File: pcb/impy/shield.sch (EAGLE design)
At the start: 117 parts, among them J1 USB-2410-06, J2 SI-60062-F, J3 5V, U1 AD5933YRS, U10 LTC3406AB, U11 23LCV1024-I/SN, U12 MIC2009A-1YM6, U13 ADG725BSU, U14 ADG725BSU, U2 ADG704BRM, U3 AD8656ARZ, U4 M24C08WMN, U5 ADG706BRU, U6 DP83848I, U7 MIC2009A-1YM6, U8 AT25DF081A-SS, U9 SST25VF080B-80-4I-S2

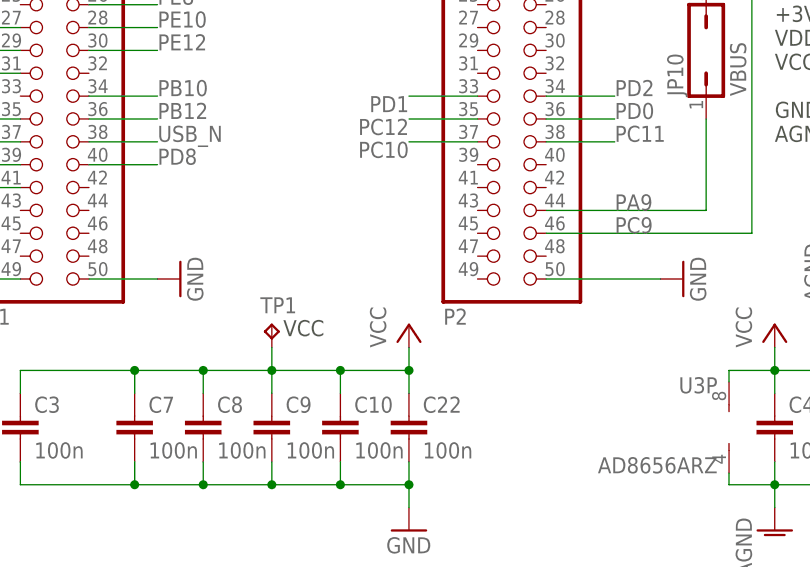
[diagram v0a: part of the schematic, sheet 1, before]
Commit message: * pcb/impy: (shield.sch) Fix missing ground connection on discovery connector.
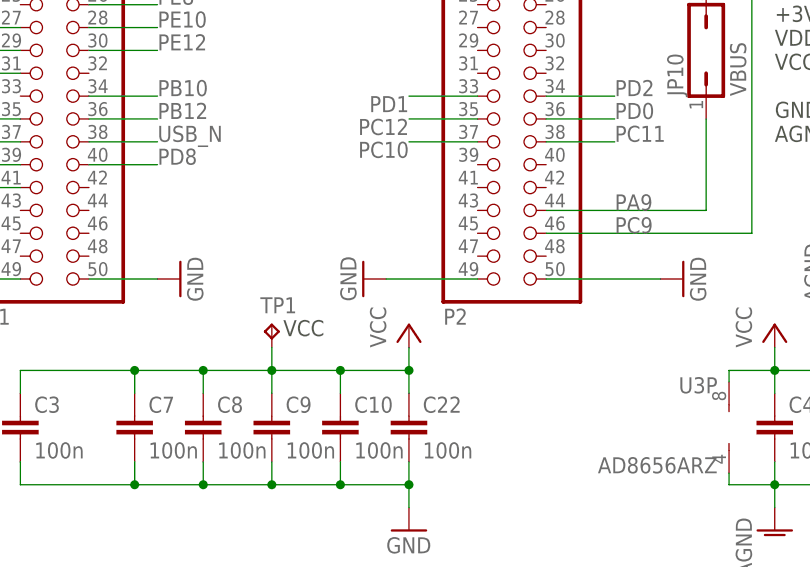
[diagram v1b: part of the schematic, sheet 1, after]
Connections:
- net GND: now also JP2.49
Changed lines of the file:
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@@
 <part name="P+36" library="supply1" deviceset="+5V" device=""/>
 <part name="VDD7" library="supply1" deviceset="VDD" device=""/>
+<part name="GND45" library="supply1" deviceset="GND" device=""/>
 </parts>
 <sheets>
@@
 <attribute name="VALUE" x="-2.54" y="17.78" size="1.778" layer="96" rot="MR180"/>
 </instance>
+<instance part="GND45" gate="1" x="58.42" y="20.32" rot="R270"/>
 </instances>
 <busses>
@@
 <wire x1="200.66" y1="-5.08" x2="200.66" y2="0" width="0.1524" layer="91"/>
 </segment>
+<segment>
+<pinref part="GND45" gate="1" pin="GND"/>
+<pinref part="JP2" gate="A" pin="49"/>
+<wire x1="60.96" y1="20.32" x2="71.12" y2="20.32" width="0.1524" layer="91"/>
+</segment>
 </net>

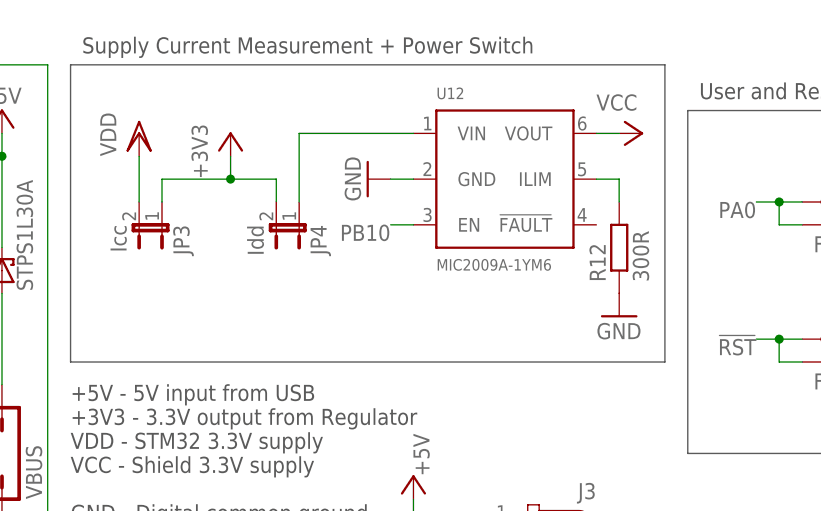
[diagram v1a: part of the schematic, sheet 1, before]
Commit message: * pcb/impy: (shield.sch) Move Icc measurement jumper after switch for easier layout.
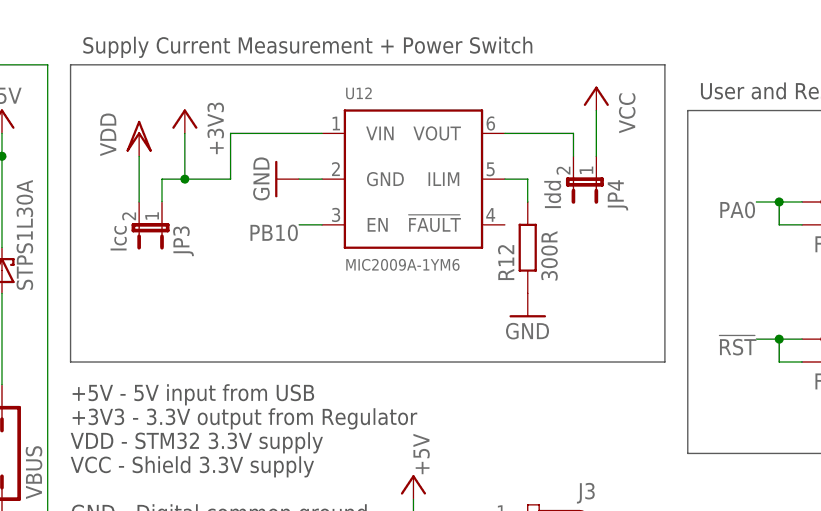
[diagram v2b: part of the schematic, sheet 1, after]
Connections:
- net +3V3: now also U12.VIN; no longer JP4.2
- net N$36: now also JP4.2, U12.VOUT; no longer JP4.1, U12.VIN
- net VCC: now also JP4.1; no longer U12.VOUT
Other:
- moved on the sheet: JP4, R12, U12
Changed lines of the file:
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@@
 <instance part="GND9" gate="1" x="60.96" y="81.28" rot="R270"/>
 <instance part="JP3" gate="A" x="114.3" y="71.12" rot="R180"/>
-<instance part="JP4" gate="A" x="129.54" y="71.12" rot="R180"/>
-<instance part="P+5" gate="VCC" x="167.64" y="81.28" smashed="yes" rot="R270">
-<attribute name="VALUE" x="162.56" y="83.82" size="1.778" layer="96"/>
+<instance part="JP4" gate="A" x="162.56" y="76.2" rot="R180"/>
+<instance part="P+5" gate="VCC" x="162.56" y="86.36" smashed="yes" rot="MR0">
+<attribute name="VALUE" x="165.1" y="81.28" size="1.778" layer="96" rot="MR90"/>
 </instance>
-<instance part="+3V3" gate="G$1" x="121.92" y="81.28"/>
+<instance part="+3V3" gate="G$1" x="116.84" y="83.82" rot="MR0"/>
 <instance part="VDD4" gate="G$1" x="111.76" y="81.28"/>
 <instance part="SJ1" gate="1" x="119.38" y="27.94"/>
@@
 <instance part="J3" gate="G$1" x="154.94" y="35.56" rot="MR0"/>
 <instance part="GND39" gate="1" x="147.32" y="27.94"/>
-<instance part="U12" gate="G$1" x="152.4" y="76.2"/>
-<instance part="GND35" gate="1" x="137.16" y="76.2" rot="R270"/>
+<instance part="U12" gate="G$1" x="142.24" y="76.2"/>
+<instance part="GND35" gate="1" x="127" y="76.2" rot="R270"/>
 <instance part="D1" gate="G$1" x="96.52" y="66.04" rot="R90"/>
-<instance part="R12" gate="G$1" x="165.1" y="68.58" smashed="yes" rot="R90">
-<attribute name="NAME" x="163.6014" y="64.77" size="1.778" layer="95" rot="R90"/>
-<attribute name="VALUE" x="168.402" y="64.77" size="1.778" layer="96" rot="R90"/>
+<instance part="R12" gate="G$1" x="154.94" y="68.58" smashed="yes" rot="R90">
+<attribute name="NAME" x="153.4414" y="64.77" size="1.778" layer="95" rot="R90"/>
+<attribute name="VALUE" x="158.242" y="64.77" size="1.778" layer="96" rot="R90"/>
 </instance>
-<instance part="GND40" gate="1" x="165.1" y="60.96"/>
+<instance part="GND40" gate="1" x="154.94" y="60.96"/>
 <instance part="U10" gate="G$1" x="167.64" y="15.24"/>
 <instance part="R14" gate="G$1" x="187.96" y="15.24" smashed="yes">
@@
 <pinref part="U12" gate="G$1" pin="GND"/>
 <pinref part="GND35" gate="1" pin="GND"/>
-<wire x1="142.24" y1="76.2" x2="139.7" y2="76.2" width="0.1524" layer="91"/>
+<wire x1="132.08" y1="76.2" x2="129.54" y2="76.2" width="0.1524" layer="91"/>
 </segment>
 <segment>
@@
 <wire x1="114.3" y1="73.66" x2="114.3" y2="76.2" width="0.1524" layer="91"/>
 <pinref part="+3V3" gate="G$1" pin="+3V3"/>
-<wire x1="114.3" y1="76.2" x2="121.92" y2="76.2" width="0.1524" layer="91"/>
-<wire x1="121.92" y1="76.2" x2="121.92" y2="78.74" width="0.1524" layer="91"/>
-<pinref part="JP4" gate="A" pin="2"/>
-<wire x1="121.92" y1="76.2" x2="127" y2="76.2" width="0.1524" layer="91"/>
-<wire x1="127" y1="76.2" x2="127" y2="73.66" width="0.1524" layer="91"/>
-<junction x="121.92" y="76.2"/>
+<wire x1="114.3" y1="76.2" x2="116.84" y2="76.2" width="0.1524" layer="91"/>
+<wire x1="116.84" y1="76.2" x2="116.84" y2="81.28" width="0.1524" layer="91"/>
+<wire x1="116.84" y1="76.2" x2="121.92" y2="76.2" width="0.1524" layer="91"/>
+<junction x="116.84" y="76.2"/>
+<pinref part="U12" gate="G$1" pin="VIN"/>
+<wire x1="132.08" y1="81.28" x2="121.92" y2="81.28" width="0.1524" layer="91"/>
+<wire x1="121.92" y1="81.28" x2="121.92" y2="76.2" width="0.1524" layer="91"/>
 </segment>
 <segment>
@@
 <segment>
 <pinref part="P+5" gate="VCC" pin="VCC"/>
-<pinref part="U12" gate="G$1" pin="VOUT"/>
-<wire x1="165.1" y1="81.28" x2="162.56" y2="81.28" width="0.1524" layer="91"/>
+<pinref part="JP4" gate="A" pin="1"/>
+<wire x1="162.56" y1="83.82" x2="162.56" y2="78.74" width="0.1524" layer="91"/>
 </segment>
 </net>
@@
 </segment>
 </net>
-<net name="N$36" class="1">
-<segment>
-<pinref part="U12" gate="G$1" pin="VIN"/>
-<pinref part="JP4" gate="A" pin="1"/>
-<wire x1="142.24" y1="81.28" x2="129.54" y2="81.28" width="0.1524" layer="91"/>
-<wire x1="129.54" y1="81.28" x2="129.54" y2="73.66" width="0.1524" layer="91"/>
-</segment>
-</net>
 <net name="PB10" class="0">
 <segment>
@@
 <segment>
 <pinref part="U12" gate="G$1" pin="EN"/>
-<wire x1="142.24" y1="71.12" x2="139.7" y2="71.12" width="0.1524" layer="91"/>
-<label x="139.7" y="71.12" size="1.778" layer="95" rot="R180"/>
+<wire x1="132.08" y1="71.12" x2="129.54" y2="71.12" width="0.1524" layer="91"/>
+<label x="129.54" y="71.12" size="1.778" layer="95" rot="R180"/>
 </segment>
 </net>
@@
 <pinref part="U12" gate="G$1" pin="ILIM"/>
 <pinref part="R12" gate="G$1" pin="2"/>
-<wire x1="162.56" y1="76.2" x2="165.1" y2="76.2" width="0.1524" layer="91"/>
-<wire x1="165.1" y1="76.2" x2="165.1" y2="73.66" width="0.1524" layer="91"/>
+<wire x1="152.4" y1="76.2" x2="154.94" y2="76.2" width="0.1524" layer="91"/>
+<wire x1="154.94" y1="76.2" x2="154.94" y2="73.66" width="0.1524" layer="91"/>
 </segment>
 </net>
@@
 </segment>
 </net>
+<net name="N$36" class="0">
+<segment>
+<pinref part="U12" gate="G$1" pin="VOUT"/>
+<pinref part="JP4" gate="A" pin="2"/>
+<wire x1="152.4" y1="81.28" x2="160.02" y2="81.28" width="0.1524" layer="91"/>
+<wire x1="160.02" y1="81.28" x2="160.02" y2="78.74" width="0.1524" layer="91"/>
+</segment>
+</net>

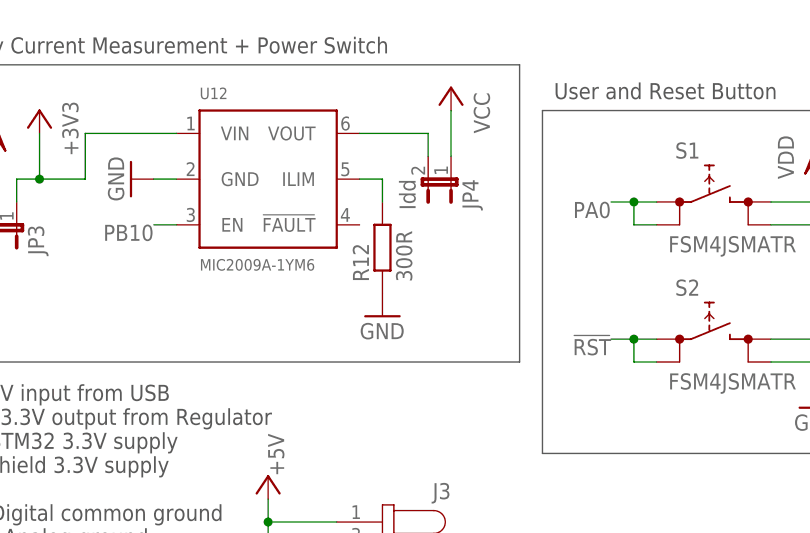
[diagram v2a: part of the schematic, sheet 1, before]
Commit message: * pcb/impy: (shield.sch) Change value of main power switch current limit resistor (to 510R which sets a 400mA limit). This switch does not carry the USB power, so the limit need not be that high.
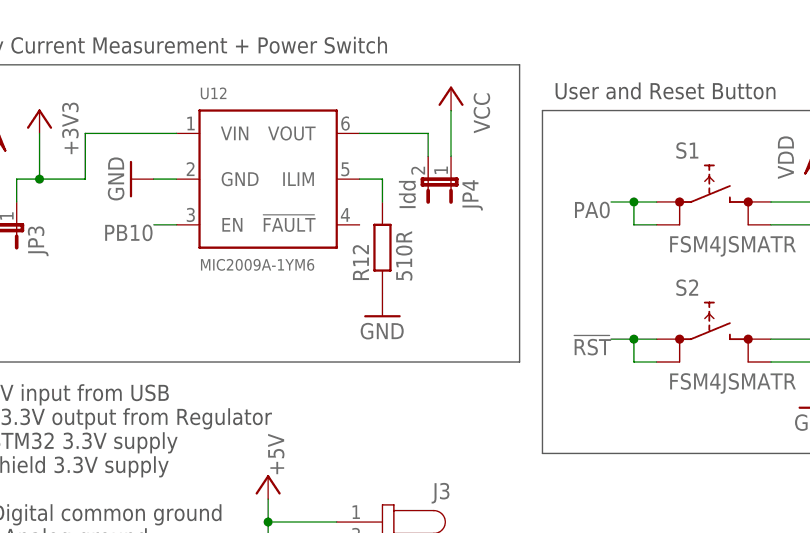
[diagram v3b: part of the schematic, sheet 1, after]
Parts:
- R12: value 300R -> 510R
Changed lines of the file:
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@@
 <part name="GND35" library="supply1" deviceset="GND" device=""/>
 <part name="D1" library="parts" deviceset="STPS1L30" device="A"/>
-<part name="R12" library="rcl" deviceset="R-EU_" device="R0603" value="300R"/>
+<part name="R12" library="rcl" deviceset="R-EU_" device="R0603" value="510R"/>
 <part name="GND40" library="supply1" deviceset="GND" device=""/>
 <part name="GND41" library="supply1" deviceset="GND" device=""/>

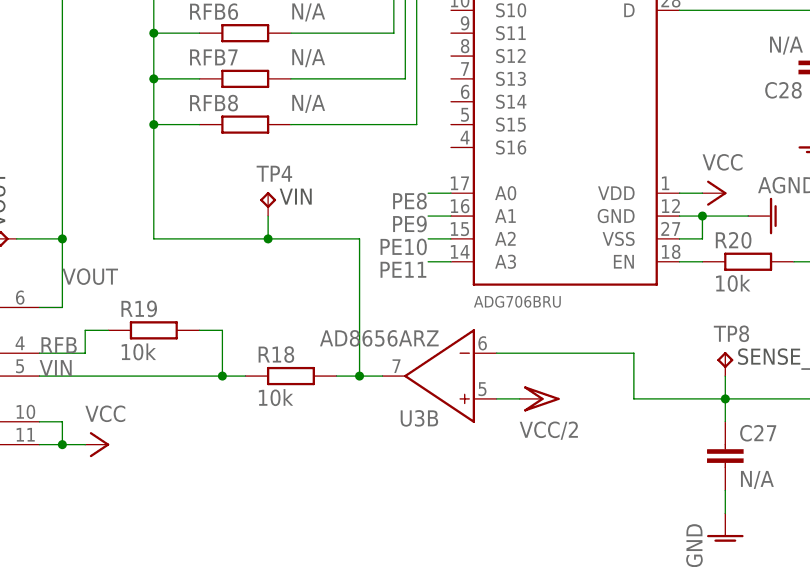
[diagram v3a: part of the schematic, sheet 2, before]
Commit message: * pcb/impy: (shield.sch) Remove unnecessary feedback resistor selection signal (PE11).   (shield.brd) Remove PE11 trace and straighten some other ones.
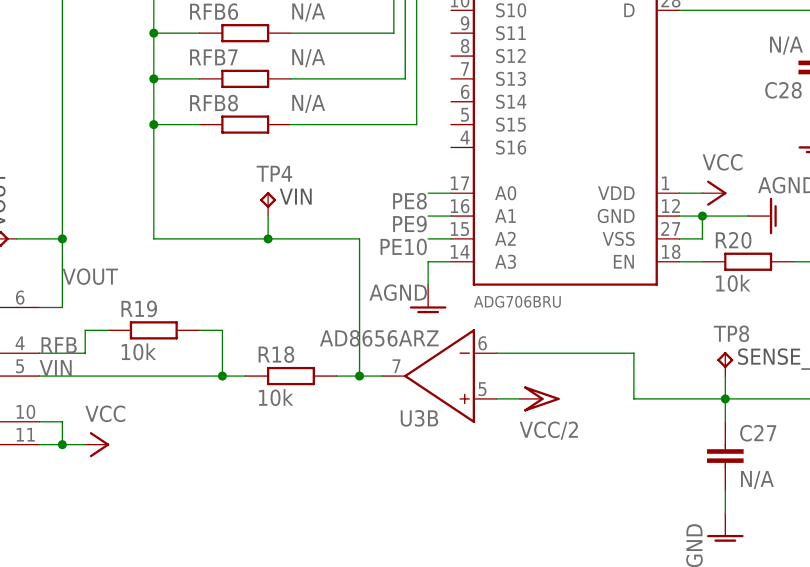
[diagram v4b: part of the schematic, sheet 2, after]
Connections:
- net AGND: now also U5.A3
- net PE11: no longer U5.A3
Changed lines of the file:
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@@
 <part name="VDD7" library="supply1" deviceset="VDD" device=""/>
 <part name="GND45" library="supply1" deviceset="GND" device=""/>
+<part name="AGND15" library="supply1" deviceset="AGND" device=""/>
 </parts>
 <sheets>
@@
 <instance part="AGND14" gate="VR1" x="35.56" y="81.28" rot="MR0"/>
 <instance part="R20" gate="G$1" x="147.32" y="58.42"/>
+<instance part="AGND15" gate="VR1" x="111.76" y="53.34" smashed="yes">
+<attribute name="VALUE" x="111.76" y="55.88" size="1.778" layer="96" rot="R180"/>
+</instance>
 </instances>
 <busses>
@@
 <pinref part="TP11" gate="G$1" pin="TP"/>
 <wire x1="35.56" y1="83.82" x2="35.56" y2="86.36" width="0.1524" layer="91"/>
+</segment>
+<segment>
+<pinref part="U5" gate="G$1" pin="A3"/>
+<pinref part="AGND15" gate="VR1" pin="AGND"/>
+<wire x1="114.3" y1="58.42" x2="111.76" y2="58.42" width="0.1524" layer="91"/>
+<wire x1="111.76" y1="58.42" x2="111.76" y2="55.88" width="0.1524" layer="91"/>
 </segment>
 </net>
@@
 </segment>
 </net>
-<net name="PE11" class="0">
-<segment>
-<pinref part="U5" gate="G$1" pin="A3"/>
-<wire x1="111.76" y1="58.42" x2="114.3" y2="58.42" width="0.1524" layer="91"/>
-<label x="111.76" y="58.42" size="1.778" layer="95" rot="R180"/>
-</segment>
-</net>

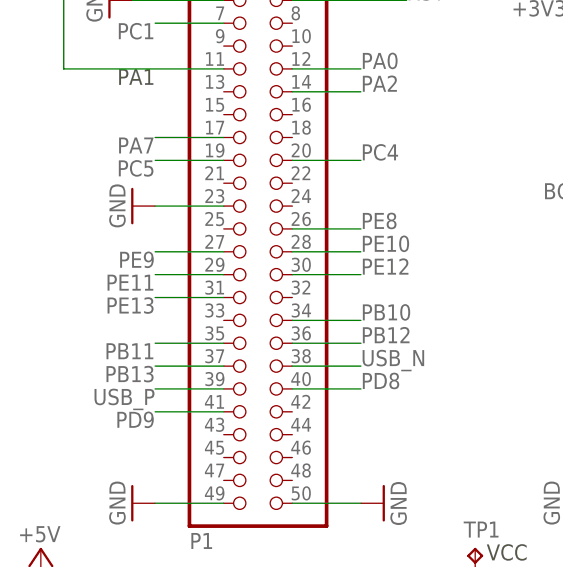
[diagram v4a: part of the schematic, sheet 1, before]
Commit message: * pcb/impy: (shield.sch) Remove PE11 from discovery board header.   (shield.brd) Move some traces in preparation for feedback mux selection signal change.
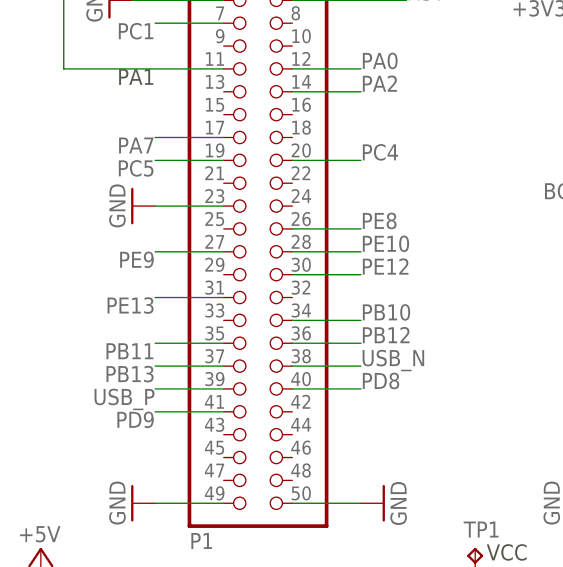
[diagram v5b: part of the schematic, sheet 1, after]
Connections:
- removed net PE11: JP1.29
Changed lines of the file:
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@@
-</segment>
-</net>
-<net name="PE11" class="0">
-<segment>
-<pinref part="JP1" gate="A" pin="29"/>
-<wire x1="20.32" y1="45.72" x2="12.7" y2="45.72" width="0.1524" layer="91"/>
-<label x="12.7" y="45.72" size="1.778" layer="95" rot="R180"/>
 </segment>
 </net>
